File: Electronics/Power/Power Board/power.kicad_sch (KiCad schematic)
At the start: 73 parts, among them IC203 MP28167GQ-A-Z, IC204 TPS563202DRLR, IC206 TPS563202DRLR, IC3 INA219AIDR, J10 Conn_01x02_Pin, J11 Conn_01x02_Pin, J2 Screw_Terminal_01x02, J202 XT60PW-M, J209 XT60PW-F, J9 Conn_01x02_Pin, Q201 PMOS, SW201 SW_SPDT

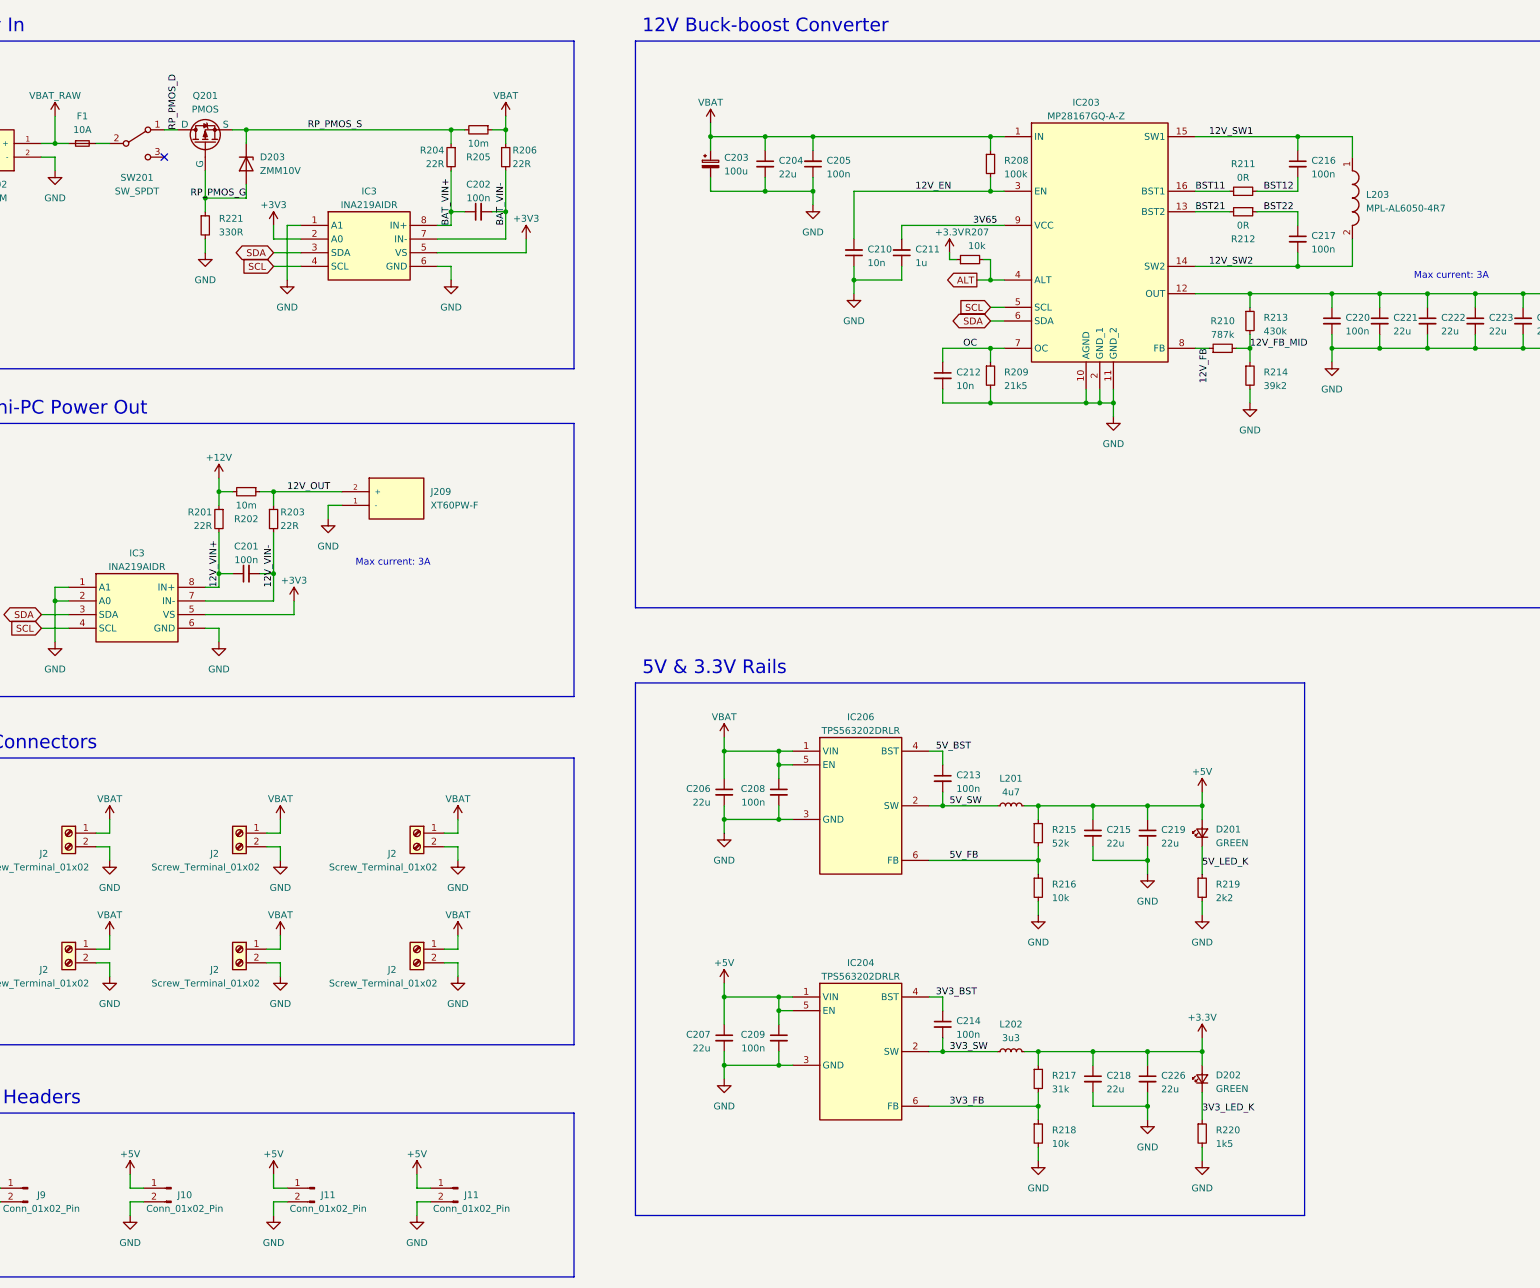
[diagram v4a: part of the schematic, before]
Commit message: PCB layout progress, spice simulations for power board
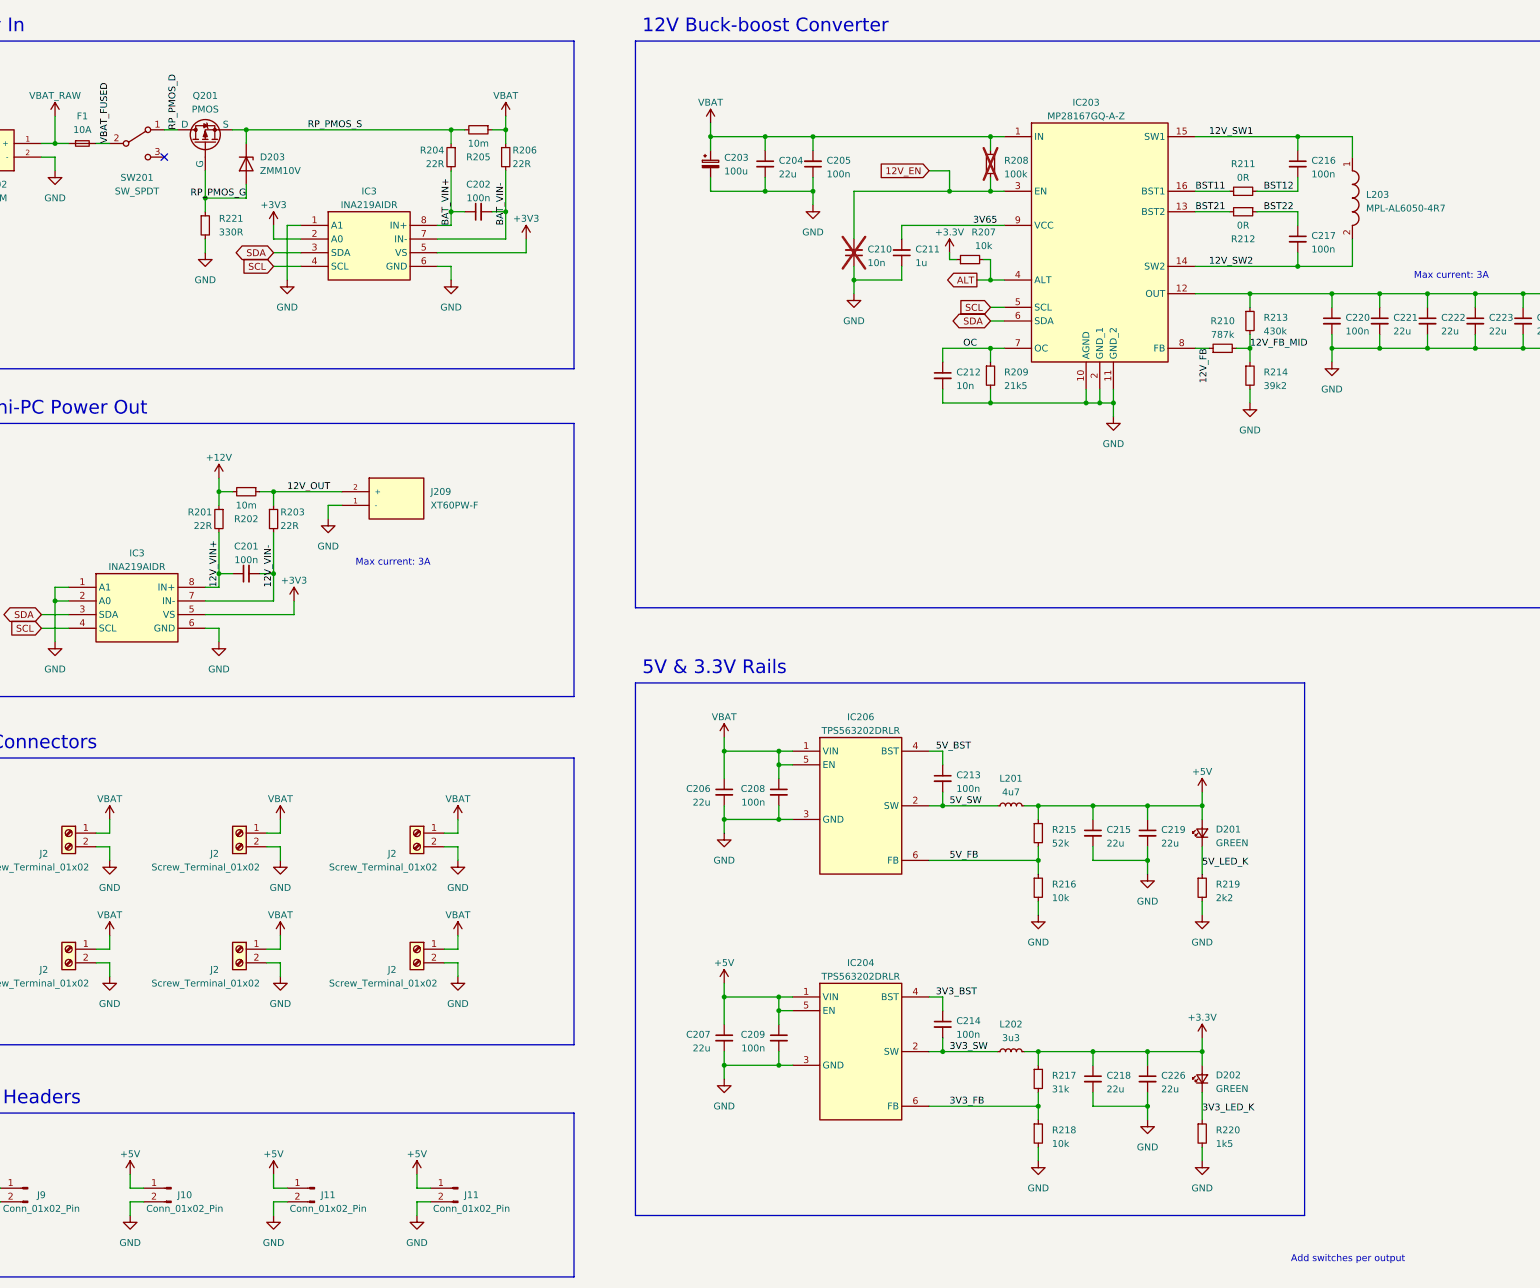
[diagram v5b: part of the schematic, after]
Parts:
- C210, R208: now not fitted; now left out of the parts list
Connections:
- net VBAT_FUSED: now reaches F1.2, SW201.2 (B)
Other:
- note added: "Add switches per output"
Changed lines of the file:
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@@
   (junction (at 106.68 44.45) (diameter 0) (color 0 0 0 0)
   )
+  (junction (at 237.49 55.88) (diameter 0) (color 0 0 0 0)
+  )
   (junction (at 203.2 45.72) (diameter 0) (color 0 0 0 0)
   )
@@
     (stroke (width 0) (type default))
   )
+  (wire (pts (xy 237.49 55.88) (xy 245.11 55.88))
+    (stroke (width 0) (type default))
+  )
   (polyline (pts (xy 46.99 99.06) (xy 167.64 99.06))
     (stroke (width 0) (type default))
@@
     (stroke (width 0) (type default))
   )
+  (wire (pts (xy 233.68 52.07) (xy 237.49 52.07))
+    (stroke (width 0) (type default))
+  )
   (wire (pts (xy 144.78 69.85) (xy 144.78 72.39))
     (stroke (width 0) (type default))
@@
     (stroke (width 0) (type default))
   )
+  (wire (pts (xy 237.49 52.07) (xy 237.49 55.88))
+    (stroke (width 0) (type default))
+  )
   (wire (pts (xy 111.76 67.31) (xy 116.84 67.31))
     (stroke (width 0) (type default))
@@
     (stroke (width 0) (type default))
   )
-  (wire (pts (xy 219.71 55.88) (xy 245.11 55.88))
+  (wire (pts (xy 219.71 55.88) (xy 237.49 55.88))
     (stroke (width 0) (type default))
   )
@@
     (effects (font (size 1.27 1.27)) (justify left bottom))
   )
+  (text "Add switches per output" (at 300.99 255.27 0)
+    (effects (font (size 1.27 1.27)) (justify left bottom))
+  )
   (text "12V Buck-boost Converter" (at 180.34 26.67 0)
     (effects (font (size 2.54 2.54)) (justify left bottom))
@@
     (effects (font (size 1.27 1.27)) (justify left bottom))
   )
-  (label "12V_EN" (at 231.14 55.88 0) (fields_autoplaced)
-    (effects (font (size 1.27 1.27)) (justify left bottom))
-  )
   (label "3V3_FB" (at 237.49 226.06 0) (fields_autoplaced)
     (effects (font (size 1.27 1.27)) (justify left bottom))
@@
     (effects (font (size 1.27 1.27)) (justify left bottom))
   )
+  (label "VBAT_FUSED" (at 81.28 46.99 90) (fields_autoplaced)
+    (effects (font (size 1.27 1.27)) (justify left bottom))
+  )
   (label "3V65" (at 246.38 62.23 180) (fields_autoplaced)
     (effects (font (size 1.27 1.27)) (justify right bottom))
@@
     (effects (font (size 1.27 1.27)) (justify left bottom))
   )
+  (global_label "12V_EN" (shape input) (at 233.68 52.07 180) (fields_autoplaced)
+    (effects (font (size 1.27 1.27)) (justify right))
+    (property "Intersheetrefs" "${INTERSHEET_REFS}" (at 223.8195 52.07 0)
+      (effects (font (size 1.27 1.27)) (justify right) hide)
+    )
+  )
   (global_label "SCL" (shape input) (at 68.58 137.16 180) (fields_autoplaced)
     (effects (font (size 1.27 1.27)) (justify right))
@@
   )
   (symbol (lib_id "Device:R_Small") (at 245.11 50.8 0) (unit 1)
-    (in_bom yes) (on_board yes) (dnp no) (fields_autoplaced)
+    (in_bom no) (on_board yes) (dnp yes) (fields_autoplaced)
     (property "Reference" "R208" (at 247.65 50.165 0)
       (effects (font (size 1.27 1.27)) (justify left))
@@
   )
   (symbol (lib_id "Device:C_Small") (at 219.71 67.31 180) (unit 1)
-    (in_bom yes) (on_board yes) (dnp no) (fields_autoplaced)
+    (in_bom no) (on_board yes) (dnp yes) (fields_autoplaced)
     (property "Reference" "C210" (at 222.25 66.6686 0)
       (effects (font (size 1.27 1.27)) (justify right))
@@
   (symbol (lib_id "Device:R_Small") (at 241.3 68.58 90) (unit 1)
     (in_bom yes) (on_board yes) (dnp no)
-    (property "Reference" "R207" (at 242.57 63.5 90)
+    (property "Reference" "R207" (at 243.84 63.5 90)
       (effects (font (size 1.27 1.27)))
     )
-    (property "Value" "10k" (at 242.57 66.04 90)
+    (property "Value" "10k" (at 243.84 66.04 90)
       (effects (font (size 1.27 1.27)))
     )

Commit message: Implemented power supply selector
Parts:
- removed Q201: PMOS, symbol Simulation_SPICE:PMOS
- removed R205: 10m, Resistor_SMD:R_0402_1005Metric, symbol Device:R_Small
- added C203, C231: 1u, Capacitor_SMD:C_0402_1005Metric, symbol Device:C_Small
- added C205, C206: 100n, Capacitor_SMD:C_0402_1005Metric, symbol Device:C_Small
- added D201, D208: ZMM16V, Diode_SMD:D_MiniMELF, symbol Diode:ZMMxx
- added D203, D209: ZMM4V7, Diode_SMD:D_MiniMELF, symbol Diode:ZMMxx
- added IC202, IC208: TLV1805DBVR, MSL Footprints:SOT95P280X145-6N, symbol TLV1805DBVR:TLV1805DBVR
- added Q201, Q202, Q203, Q204, Q205: DMP3013SFV-7, MSL Footprints:DMP3013SFV7, symbol DMP3013SFV-7:DMP3013SFV-7
- added R208, R234: 100k, Resistor_SMD:R_0402_1005Metric, symbol Device:R_Small
- added R211, R213, R215, R235: 22R, Resistor_SMD:R_0402_1005Metric, symbol Device:R_Small
- added R214: 10m, Resistor_SMD:R_0402_1005Metric, symbol Device:R_Small
- added R230, R233: 10k, Resistor_SMD:R_0402_1005Metric, symbol Device:R_Small
- added R231: 4k7, Resistor_SMD:R_0402_1005Metric, symbol Device:R_Small
- added R232: 1k, Resistor_SMD:R_0402_1005Metric, symbol Device:R_Small
- J201: renamed from J209; footprint Connector_AMASS:AMASS_XT60PW-F_1x02_P7.20mm_Horizontal -> MSL Footprints:AMASS_XT60PW-F_1x02_P7.20mm_Horizontal
- J203: renamed from J202; footprint Connector_AMASS:AMASS_XT60PW-M_1x02_P7.20mm_Horizontal -> MSL Footprints:AMASS_XT60PW-M_1x02_P7.20mm_Horizontal
- R204: value 22R -> 4k7
- R206: value 22R -> 1k
- renumbered C203 to C207, C204 to C208, C205 to C209, C206 to C213, C207 to C214, C208 to C215, C209 to C216, C216 to C217, C217 to C218, C213 to C219, C214 to C220, C220 to C221, C221 to C222, C222 to C223, C215 to C224, C218 to C225, C223 to C226, C224 to C227, C219 to C228, C226 to C229, C225 to C230, D203 to D205, D201 to D206, D202 to D207, IC203 to IC205, IC204 to IC207, L203 to L201, L201 to L202, L202 to L203, R221 to R210, R207 to R216, R208 to R217, R209 to R218, R210 to R219, R211 to R220, R212 to R221, R213 to R222, R214 to R223, R215 to R224, R216 to R225, R217 to R226, R218 to R227, R219 to R228, R220 to R229
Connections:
- net +3V3: now also C202.2, IC3.2 (A0), C206.2; no longer IC3.2 (A0)
- net +5V: no longer C214.1, C216.1, IC207.1 (VIN), IC207.5 (EN)
- net GND: now also C202.1, IC3.2 (A0), J203.1 (-), R204.2, C203.2, C206.1, C231.2, D203.2 (A), D209.2 (A), IC202.2 (V-), IC208.2 (V-), R231.2; no longer IC3.2 (A0), J203.2 (-)
- net RP_PMOS_G: now also Q205.4 (G)
- net VBAT: now also D205.1 (K), D201.1 (K), D208.1 (K), Q202.5 (D_1), Q202.6 (D_2), Q202.7 (D_3), Q202.8 (D_4), Q202.9 (D_5), Q203.5 (D_1), Q203.6 (D_2), Q203.7 (D_3), Q203.8 (D_4), Q203.9 (D_5), Q205.1 (S_1), Q205.2 (S_2), Q205.3 (S_3), R230.1, R233.1; no longer C207.1, C208.1, C209.2, C213.1, C215.1, IC205.1 (IN), IC206.1 (VIN), IC206.5 (EN), J2.1 (Pin_1), J2.1 (Pin_1), J2.1 (Pin_1), J2.1 (Pin_1), J2.1 (Pin_1), J2.1 (Pin_1), R206.1, R217.1
- net VBAT_RAW: now also J203.2 (+); no longer J203.1 (+)
- removed net BAT_VIN+: C202.1, IC3.8 (IN+), R204.2
- removed net BAT_VIN-: C202.2, IC3.7 (IN-), R206.2
- net RP_PMOS_D renamed VBAT_SWITCHED
- net VBAT_SWITCHED: now also Q205.5 (D_1), Q205.6 (D_2), Q205.7 (D_3), Q205.8 (D_4), Q205.9 (D_5)
- net RP_PMOS_S renamed VBAT_SHDN_A
- net VBAT_SHDN_A: now also R206.1, D201.2 (A); no longer D205.1 (K)
- new net VBAT_COMP-: IC202.3 (-), R230.2
- new net VBAT_COMP_OUT: IC202.1, R211.1
- new net VBAT_GATE: Q201.4 (G), Q203.4 (G), R208.2, R211.2
- new net VBAT_SHDN_K: D203.1 (K), IC202.5 (SH), R206.2
- new net VBAT_SOURCE: C203.1, IC202.4 (+), IC202.6 (V+), Q201.1 (S_1), Q201.2 (S_2), Q201.3 (S_3), Q203.1 (S_1), Q203.2 (S_2), Q203.3 (S_3), R208.1
- new net VBUS_COMP-: IC208.3 (-), R233.2
- new net VBUS_COMP_OUT: IC208.1, R235.1
- new net VBUS_GATE: Q202.4 (G), Q204.4 (G), R234.2, R235.2
- new net VBUS_SHDN_A: D208.2 (A), R231.1, R232.1
- new net VBUS_SHDN_K: D209.1 (K), IC208.5 (SH), R232.2
- new net VBUS_SOURCE: C231.1, IC208.4 (+), IC208.6 (V+), Q202.1 (S_1), Q202.2 (S_2), Q202.3 (S_3), Q204.1 (S_1), Q204.2 (S_2), Q204.3 (S_3), R234.1
- new net VDD: C207.1, C208.1, C209.2, C213.1, C214.1, C215.1, C216.1, IC205.1 (IN), IC206.1 (VIN), IC206.5 (EN), IC207.1 (VIN), IC207.5 (EN), J2.1 (Pin_1), J2.1 (Pin_1), J2.1 (Pin_1), J2.1 (Pin_1), J2.1 (Pin_1), J2.1 (Pin_1), R214.1, R215.1, R217.1
- new net VDD_VIN+: C205.1, IC3.8 (IN+), R213.2
- new net VDD_VIN-: C205.2, IC3.7 (IN-), R215.2
- new net VIN: Q201.5 (D_1), Q201.6 (D_2), Q201.7 (D_3), Q201.8 (D_4), Q201.9 (D_5), Q204.5 (D_1), Q204.6 (D_2), Q204.7 (D_3), Q204.8 (D_4), Q204.9 (D_5), R213.1, R214.2
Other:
- note added: "Add switches per output Add new VBUS (and battery) TVS diodes Check zener diode resistors"
- note added: "Battery Input & Reverse Polarity Protection"
- note added: "Input Power Monitoring"
- note added: "Supply Selector, OVP & Reverse Current Protection"
- note removed: "Add switches per output"
- note removed: "Battery In"
- moved on the sheet: C201, C207, C208, C209, C210, C211, C212, C213, C214, C215, C216, C217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

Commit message: Finished power board layout
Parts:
- removed J11: Conn_01x02_Pin, Connector_PinHeader_2.54mm:PinHeader_1x02_P2.54mm_Vertical, symbol Connector:Conn_01x02_Pin
- removed J2 (x2): Screw_Terminal_01x02, TerminalBlock:TerminalBlock_bornier-2_P5.08mm, symbol Connector:Screw_Terminal_01x02
- added C204, C233: 120p, Capacitor_SMD:C_0402_1005Metric, symbol Device:C_Small
- added C235, C236: 100n, Capacitor_SMD:C_0402_1005Metric, symbol Device:C_Small
- added C237, C238: 1u, Capacitor_SMD:C_0402_1005Metric, symbol Device:C_Small
- added D1 (x2): BAT760-115, Diode_SMD:D_SOD-323, symbol Device:D_Schottky
- added IC3: INA219AIDR, MSL Footprints:SOIC127P600X175-8N, symbol INA219AIDR:INA219AIDR
- added J2 (x4): Screw_Terminal_01x02, TerminalBlock:TerminalBlock_bornier-2_P5.08mm, symbol Connector:Screw_Terminal_01x02
- added Q206, Q207: SSM6K513NU,LF, MSL Footprints:SSM6K513NULF, symbol SSM6K513NU_LF:SSM6K513NU,LF
- added R205, R212: 33k, Resistor_SMD:R_0402_1005Metric, symbol Device:R_Small
- added R207, R209: 100k, Resistor_SMD:R_0402_1005Metric, symbol Device:R_Small
- added R236, R238: 22R, Resistor_SMD:R_0402_1005Metric, symbol Device:R_Small
- added R237: 10m, Resistor_SMD:R_0402_1005Metric, symbol Device:R_Small
- added U201: TCKE800NA_RF, WSON10B_TOS, symbol TCKE800NA-RF:TCKE800NA_RF
- added U202: TCKE812NA_RF, WSON10B_TOS, symbol TCKE800NA-RF:TCKE812NA_RF
- added U304: TVS1800DRV, Package_SON:WSON-6-1EP_2x2mm_P0.65mm_EP1x1.6mm, symbol Power_Protection:TVS1800DRV
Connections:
- net +12V: now also U202.3 (VIN), U202.4 (VIN), U202.5 (VIN); no longer R201.1, R202.2
- net +3V3: now also C236.2, IC3.5 (VS)
- net 12V_OUT: now also D1.1 (K), J2.2 (Pin_2)
- net GND: now also C204.2, C233.2, C236.1, C237.2, C238.2, D1.2 (A), D1.2 (A), IC3.1 (A1), IC3.6 (GND), J2.1 (Pin_1), J2.2 (Pin_2), J2.2 (Pin_2), J2.2 (Pin_2), R205.2, R207.2, R209.2, R212.2, U201.11 (GND), U202.11 (GND), U304.1 (GND), U304.2 (GND), U304.3 (GND), U304.7 (GND)
- net SCL: now also IC3.4 (SCL)
- net SDA: now also IC3.2 (A0), IC3.3 (SDA)
- net VBAT: no longer D208.1 (K), Q202.5 (D_1), Q202.6 (D_2), Q202.7 (D_3), Q202.8 (D_4), Q202.9 (D_5), R233.1
- net VBAT_RAW: now also J2.1 (Pin_1)
- net VBAT_SWITCHED: now also U304.4 (IN), U304.5 (IN), U304.6 (IN)
- net VDD: now also U201.3 (VIN), U201.4 (VIN), U201.5 (VIN); no longer J2.1 (Pin_1), J2.1 (Pin_1), J2.1 (Pin_1), J2.1 (Pin_1)
- new net 12V_OUT_D: C237.1, Q207.1 (D), Q207.2 (D), Q207.5 (D), Q207.6 (D), Q207.7 (D), R201.1, R202.2
- new net 12V_OUT_DV/DT: C233.1, U202.1 (DV/DT)
- new net 12V_OUT_EN: R209.1, U202.2 (EN/UVLO)
- new net 12V_OUT_G: Q207.3 (G), U202.9 (EFET)
- new net 12V_OUT_ILIM: R212.1, U202.10 (ILIM)
- new net 12V_OUT_S: Q207.4 (S), Q207.8 (S), U202.6 (VOUT), U202.7 (VOUT), U202.8 (VOUT)
- new net VBUS: D208.1 (K), Q202.5 (D_1), Q202.6 (D_2), Q202.7 (D_3), Q202.8 (D_4), Q202.9 (D_5), R233.1
- new net VOUT: D1.1 (K), J2.1 (Pin_1), J2.1 (Pin_1), J2.1 (Pin_1), J2.1 (Pin_1), J2.1 (Pin_1), J2.1 (Pin_1), R237.1, R238.1
- new net VOUT_D: C238.1, Q206.1 (D), Q206.2 (D), Q206.5 (D), Q206.6 (D), Q206.7 (D), R236.1, R237.2
- new net VOUT_DV/DT: C204.1, U201.1 (DV/DT)
- new net VOUT_EN: R207.1, U201.2 (EN/UVLO)
- new net VOUT_G: Q206.3 (G), U201.9 (EFET)
- new net VOUT_ILIM: R205.1, U201.10 (ILIM)
- new net VOUT_S: Q206.4 (S), Q206.8 (S), U201.6 (VOUT), U201.7 (VOUT), U201.8 (VOUT)
- new net VOUT_VIN+: C235.1, IC3.8 (IN+), R236.2
- new net VOUT_VIN-: C235.2, IC3.7 (IN-), R238.2
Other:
- note added: "12V Mini-PC Power Out & Monitoring"
- note added: "Battery Input & RP Protection"
- note added: "I2C ADDR: 0x40"
- note added: "I2C ADDR: 0x41"
- note added: "I2C ADDR: 0x42"
- note added: "I2C ADDR: 0x60"
- note added: "Max input voltage 30V"
- note added: "Overvoltage and reverse current protection circuits based on TLV1805 datasheet."
- note added: "R_{ILIM} = 33k ∴ I_{LIM} = ~3A"
- note added: "Reverse polarity protection using PMOS"
- note added: "Supply Selector, OVP & RCP"
- note added: "VBAT Power Out & Monitoring"
- note added: "V_{SHDN} must be < 5.5V"
- note removed: "12V Mini-PC Power Out"
- note removed: "Add switches per output Add new VBUS (and battery) TVS diodes Check zener diode resistors"
- note removed: "Battery Input & Reverse Polarity Protection"
- note removed: "Supply Selector, OVP & Reverse Current Protection"
- moved on the sheet: C201, C202, C203, C205, C206, C207, C208, C209, C210, C211, C212, C213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
